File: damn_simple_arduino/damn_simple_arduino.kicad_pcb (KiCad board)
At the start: 2 copper layers, 53 x 68.5 mm, 28 parts, among them IC1 ATMEGA328P-P, P1 USB_B, P2 CONN_01X08, P3 CONN_01X10, P4 CONN_01X06, P5 CONN_01X08, P6 CONN_02X03, U1 FT231XS, Y1 Crystal

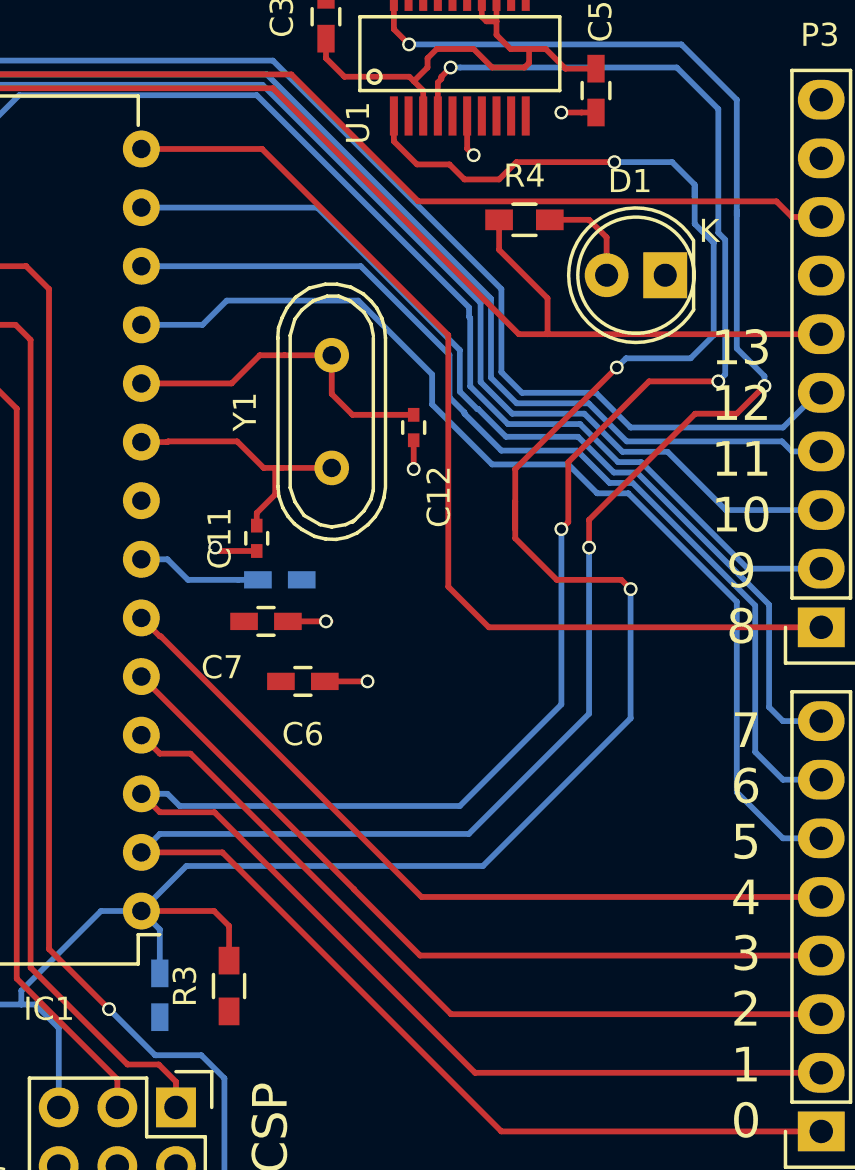
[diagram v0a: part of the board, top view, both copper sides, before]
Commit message: Updating design to AC couple the reset line to DTR, after bring-up tests.
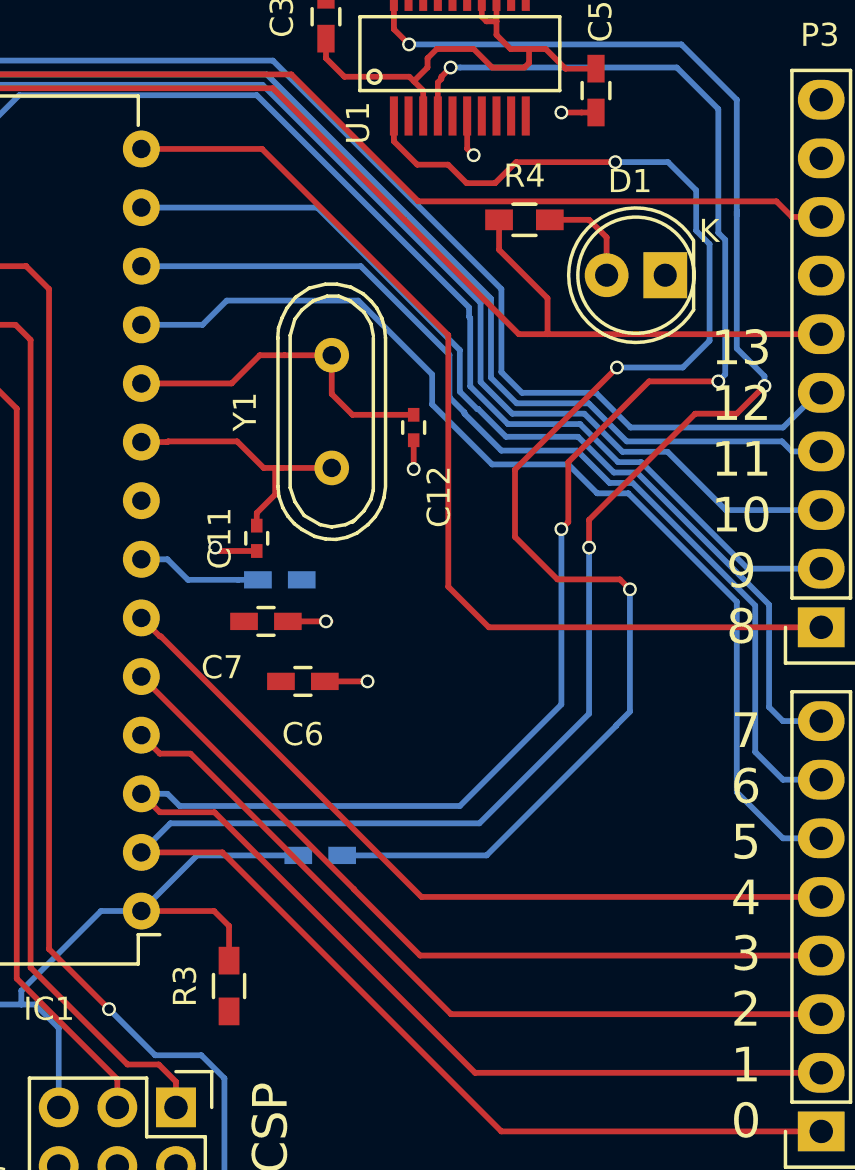
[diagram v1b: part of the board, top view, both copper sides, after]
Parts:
- moved C10 9.22 mm to (214.2, 120.1), turned to 0 degrees
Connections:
- C10 pad 2: Earth -> Net-(C10-Pad2)
- U1 pad 1: /MCU_RST -> Net-(C10-Pad2)
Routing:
- net /MCU_RST: track 132.8 -> 63.3 mm, vias 3 -> 0
- net Net-(C10-Pad2): track 0.00 -> 62.5 mm, vias 0 -> 3

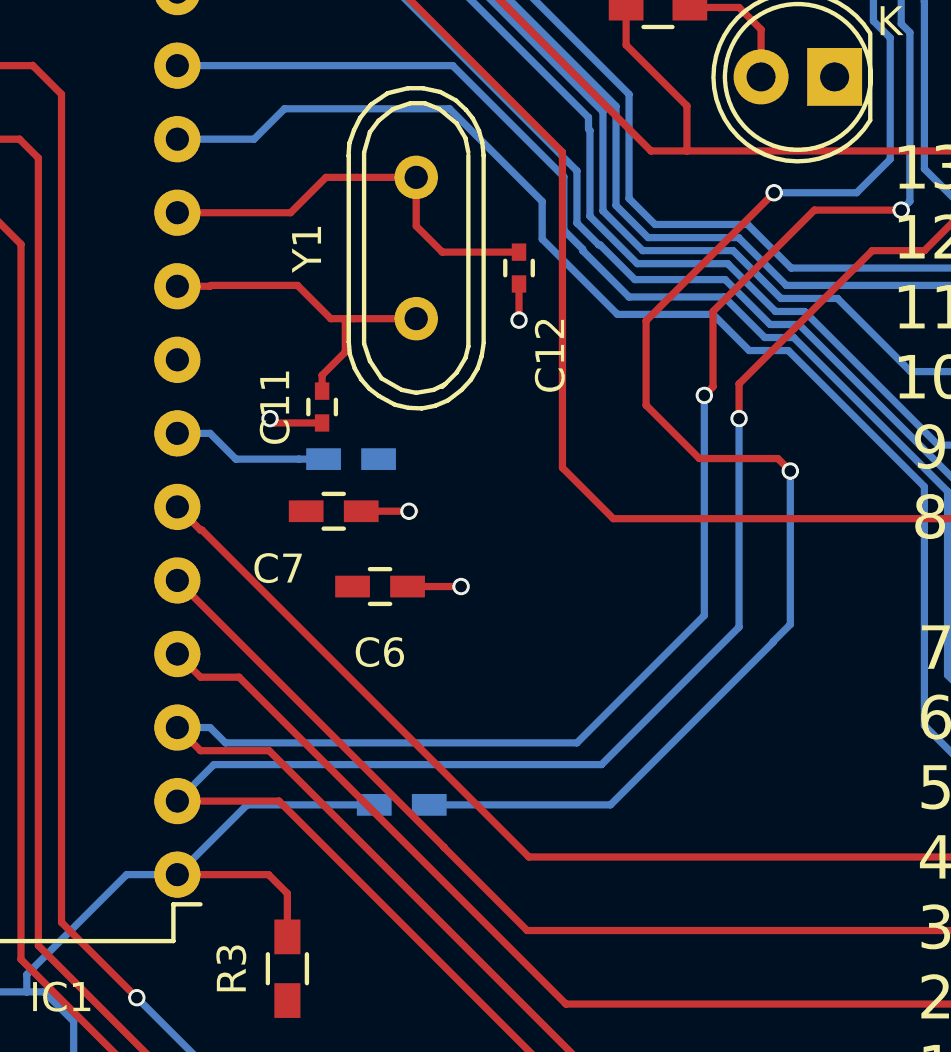
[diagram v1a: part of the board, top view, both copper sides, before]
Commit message: Updating layout with keepout zone for crystal. Also adding BOM.
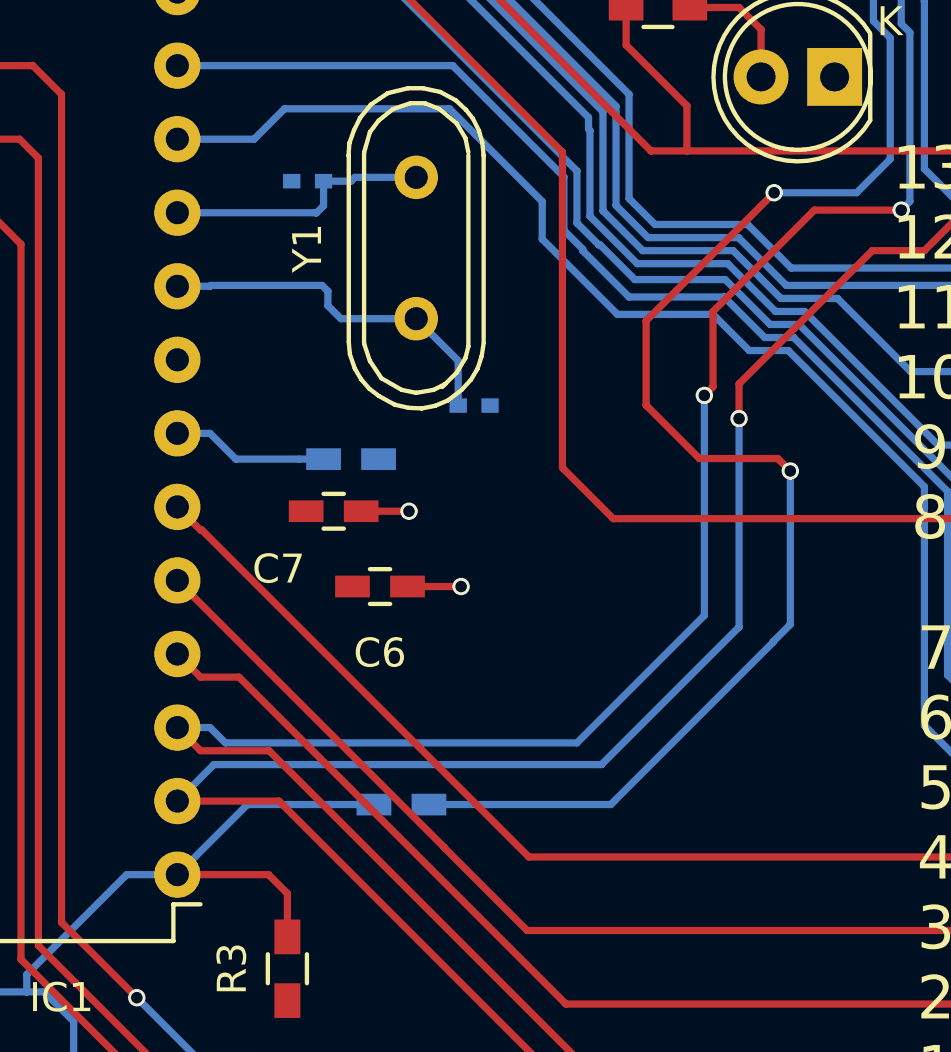
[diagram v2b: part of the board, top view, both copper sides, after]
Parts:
- C11, C12: moved to B.Cu
- moved C12 7.89 mm to (211.0, 98.5), turned to 180 degrees
- moved C11 5.25 mm to (216.7, 106.3), turned to 0 degrees
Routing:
- net Net-(C12-Pad1): track 14.4 -> 9.26 mm
- net Earth: track 21.7 -> 18.6 mm, vias 12 -> 10
- net Net-(C11-Pad1): track 11.6 -> 12.6 mm
